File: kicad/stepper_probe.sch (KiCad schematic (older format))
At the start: 49 parts, among them J1 Conn_01x04_Male, J2 Conn_01x04_Male, J3 BAT, J4 Conn_01x03_Male, J5 SWD, J6 Reset header, M1 Motor, Q1 PJA3439, SW1 SW_Push, U1 CC6920BSO-5A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

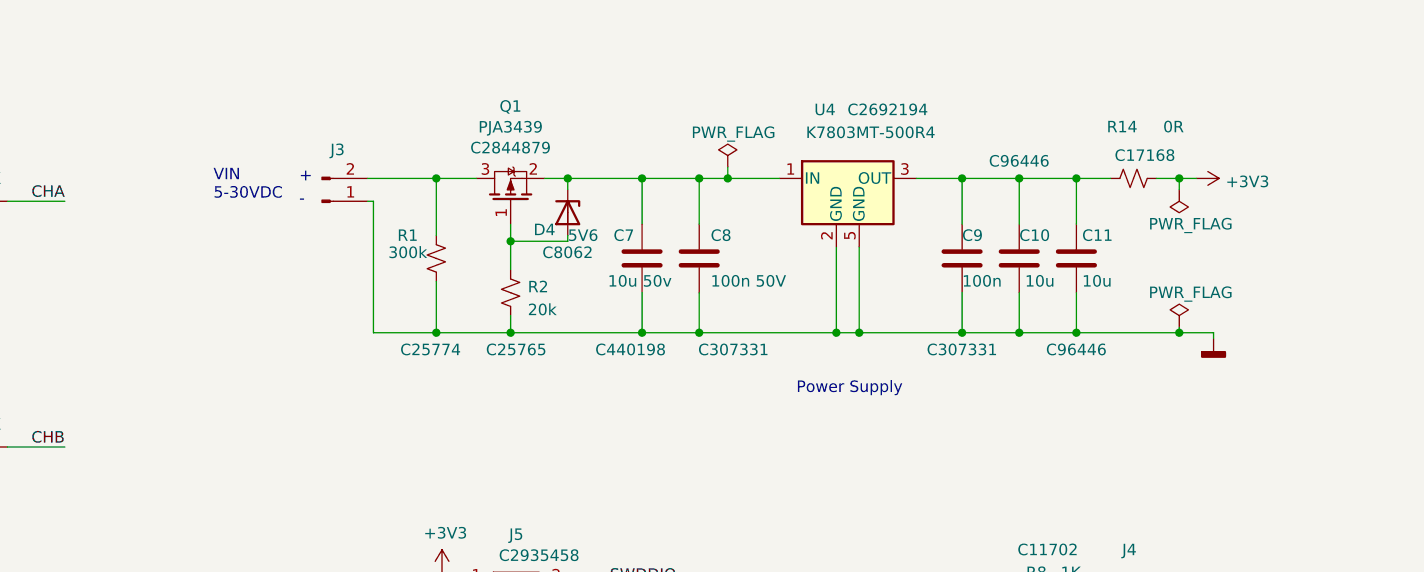
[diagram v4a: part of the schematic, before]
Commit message: Upgraded to kicad 6
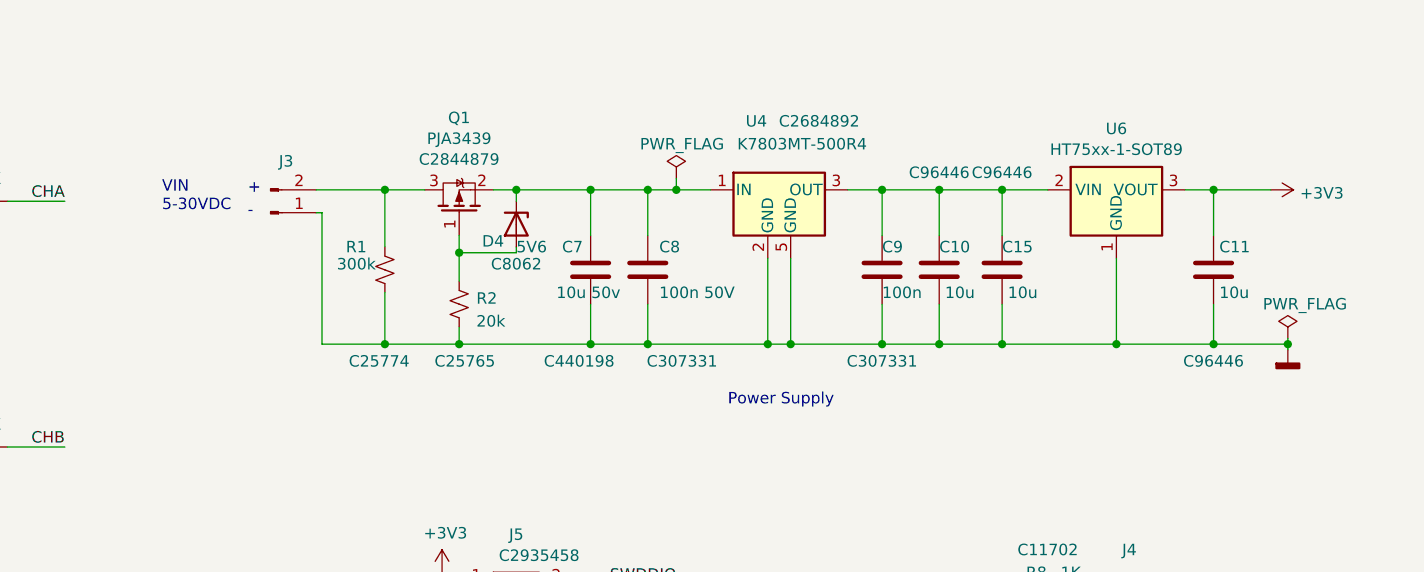
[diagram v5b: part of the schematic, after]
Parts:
- removed R14: 0R, stepper_probe:R_0402_1005Metric_Pad0.72x0.64mm_HandSolder, symbol Device:R_Small_US
- added C15: 10u, stepper_probe:C_0603_1608Metric_Pad1.08x0.95mm_HandSolder, symbol Device:C
- added U6: HT75xx-1-SOT89, Package_TO_SOT_SMD:SOT-89-3, symbol Regulator_Linear:HT75xx-1-SOT89
- U4: LCSC C2692194 -> C2684892
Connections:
- net +3V3: now also C11.1, U6.3 (VOUT)
- net GND: now also C15.2, U6.1 (GND)
- net at C10.1, C9.1, U4.3 (OUT): now also C15.1, U6.2 (VIN); no longer C11.1
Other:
- moved on the sheet: C10, C11, C7, C8, C9, D4, J3, Q1, R1, R2, U4
